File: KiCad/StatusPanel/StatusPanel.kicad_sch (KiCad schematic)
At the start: 1 part, among them U1 CC56-12EWA

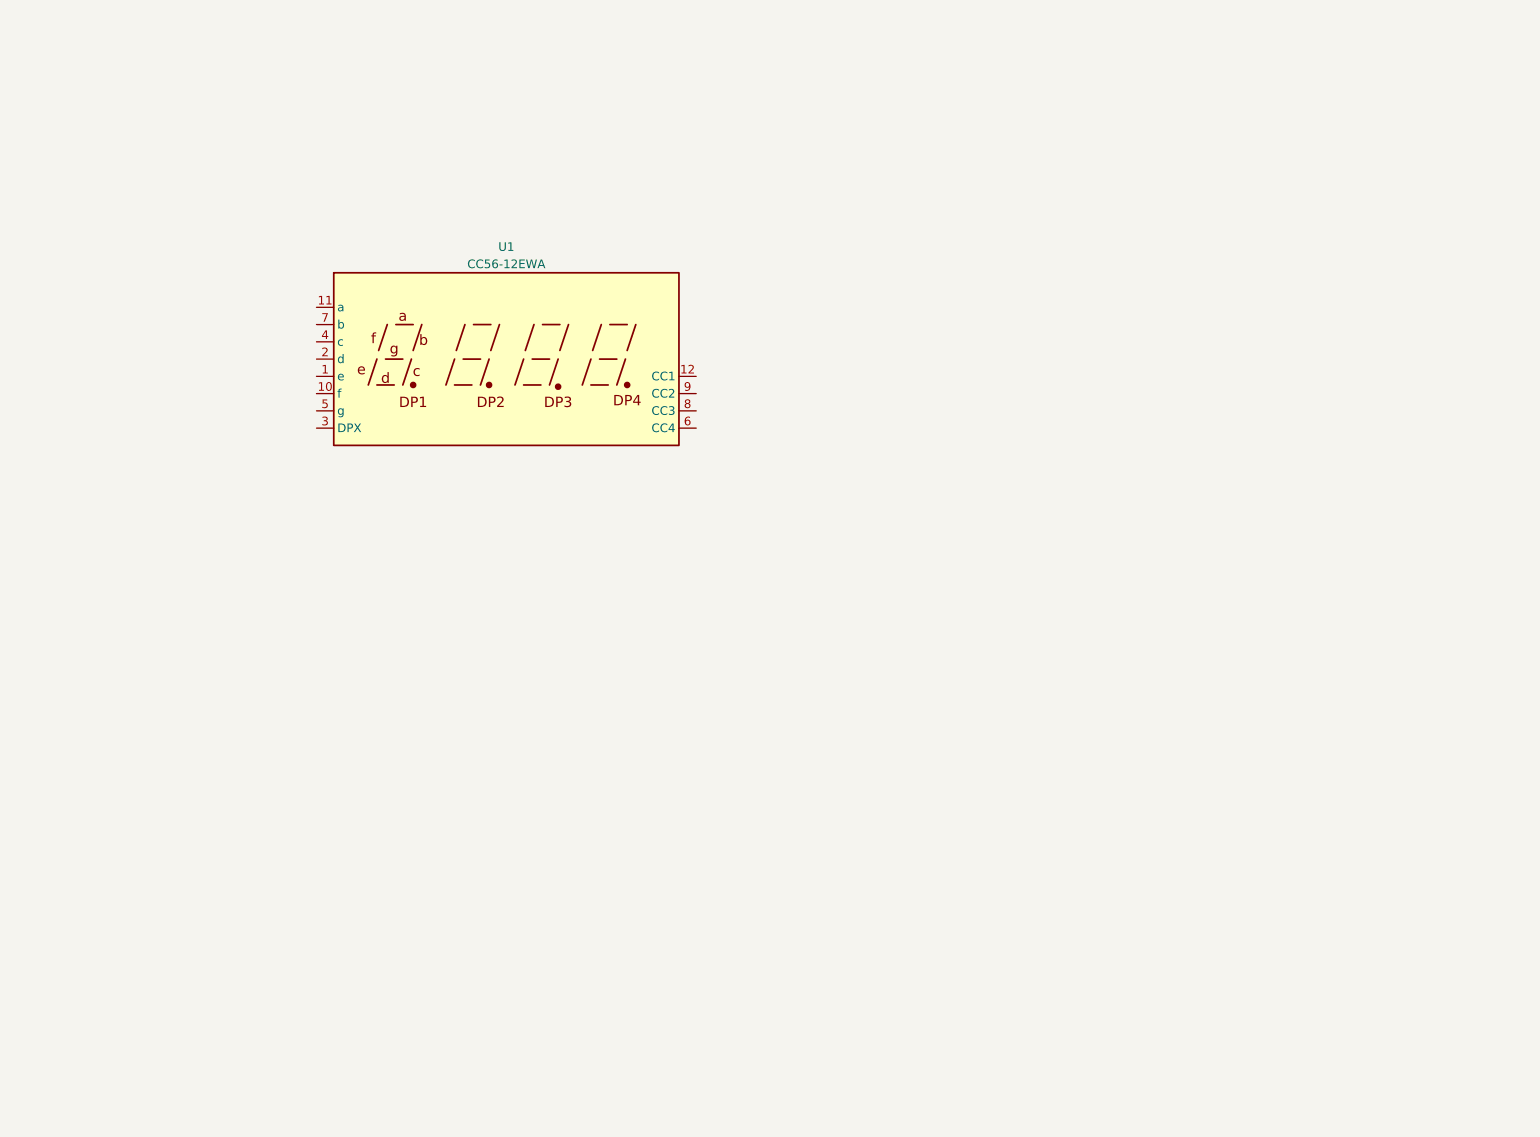
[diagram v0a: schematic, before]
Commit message: ステータスパネルの裏面に配線を追加
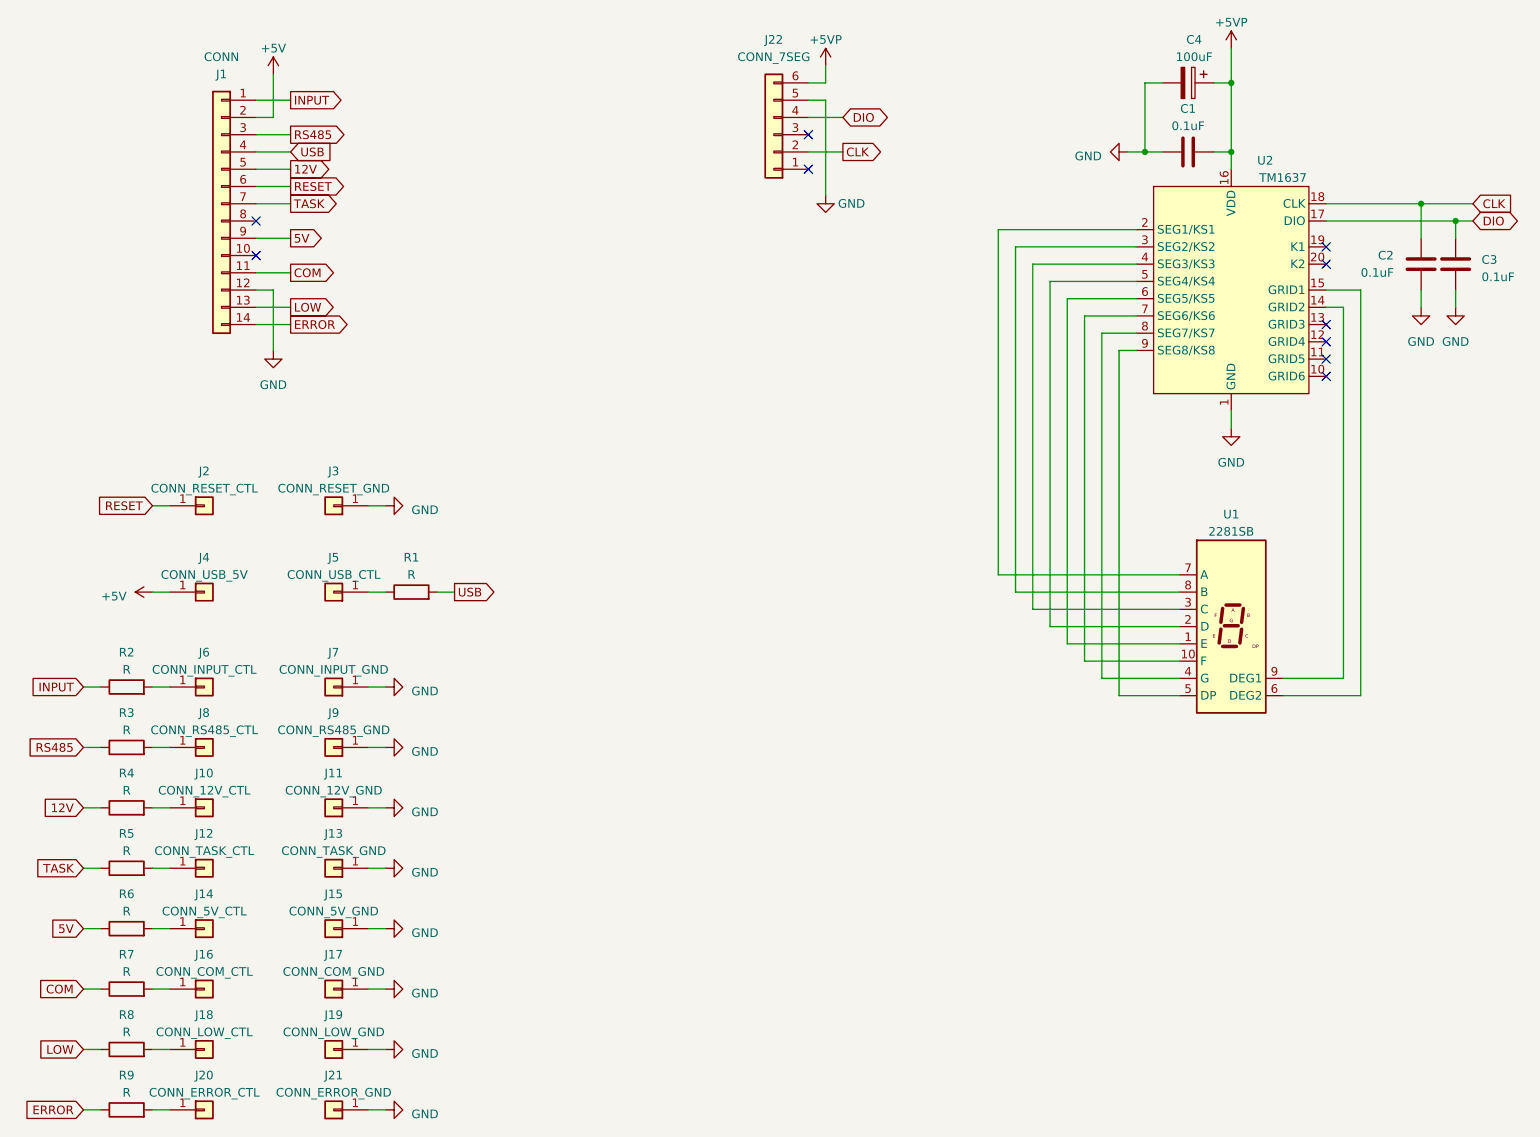
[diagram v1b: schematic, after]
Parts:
- removed U1: CC56-12EWA, Display_7Segment:CA56-12CGKWA, symbol Display_Character:CC56-12EWA
- added C1, C2, C3: 0.1uF, Capacitor_SMD:C_0603_1608Metric_Pad1.08x0.95mm_HandSolder, symbol Device:C
- added C4: 100uF, Capacitor_SMD:C_Elec_6.3x7.7, symbol Device:C_Polarized
- added J1: CONN, TSRP_Connector_Hirose:DF51A-14DP-2DS, symbol Connector_Generic:Conn_01x14
- added J10: CONN_12V_CTL, TSRP_Connector_Generic:1p, symbol Connector_Generic:Conn_01x01
- added J11: CONN_12V_GND, TSRP_Connector_Generic:1p, symbol Connector_Generic:Conn_01x01
- added J12: CONN_TASK_CTL, TSRP_Connector_Generic:1p, symbol Connector_Generic:Conn_01x01
- added J13: CONN_TASK_GND, TSRP_Connector_Generic:1p, symbol Connector_Generic:Conn_01x01
- added J14: CONN_5V_CTL, TSRP_Connector_Generic:1p, symbol Connector_Generic:Conn_01x01
- added J15: CONN_5V_GND, TSRP_Connector_Generic:1p, symbol Connector_Generic:Conn_01x01
- added J16: CONN_COM_CTL, TSRP_Connector_Generic:1p, symbol Connector_Generic:Conn_01x01
- added J17: CONN_COM_GND, TSRP_Connector_Generic:1p, symbol Connector_Generic:Conn_01x01
- added J18: CONN_LOW_CTL, TSRP_Connector_Generic:1p, symbol Connector_Generic:Conn_01x01
- added J19: CONN_LOW_GND, TSRP_Connector_Generic:1p, symbol Connector_Generic:Conn_01x01
- added J2: CONN_RESET_CTL, TSRP_Connector_Generic:1p, symbol Connector_Generic:Conn_01x01
- added J20: CONN_ERROR_CTL, TSRP_Connector_Generic:1p, symbol Connector_Generic:Conn_01x01
- added J21: CONN_ERROR_GND, TSRP_Connector_Generic:1p, symbol Connector_Generic:Conn_01x01
- added J22: CONN_7SEG, TSRP_Connector_Hirose:DF51A-6DP-2DSA, symbol Connector_Generic:Conn_01x06
- added J3: CONN_RESET_GND, TSRP_Connector_Generic:1p, symbol Connector_Generic:Conn_01x01
- added J4: CONN_USB_5V, TSRP_Connector_Generic:1p, symbol Connector_Generic:Conn_01x01
- added J5: CONN_USB_CTL, TSRP_Connector_Generic:1p, symbol Connector_Generic:Conn_01x01
- added J6: CONN_INPUT_CTL, TSRP_Connector_Generic:1p, symbol Connector_Generic:Conn_01x01
- added J7: CONN_INPUT_GND, TSRP_Connector_Generic:1p, symbol Connector_Generic:Conn_01x01
- added J8: CONN_RS485_CTL, TSRP_Connector_Generic:1p, symbol Connector_Generic:Conn_01x01
- added J9: CONN_RS485_GND, TSRP_Connector_Generic:1p, symbol Connector_Generic:Conn_01x01
- added R1, R2, R3, R4, R5, R6, R7, R8, R9: R, Resistor_SMD:R_0603_1608Metric_Pad0.98x0.95mm_HandSolder, symbol Device:R
- added U1: 2281SB, Display_7Segment:Sx39-1xxxxx, symbol Display_Character:SC39-12EWA
- added U2: TM1637, Package_SO:SOP-20_7.5x12.8mm_P1.27mm, symbol TSRP_Module:TM1637
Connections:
- new net: J6.1 (Pin_1), R2.2
- new net: J12.1 (Pin_1), R5.2
- new net: J20.1 (Pin_1), R9.2
- new net: J5.1 (Pin_1), R1.1
- new net: J14.1 (Pin_1), R6.2
- new net: J16.1 (Pin_1), R7.2
- new net: J8.1 (Pin_1), R3.2
- new net: J18.1 (Pin_1), R8.2
- new net: J10.1 (Pin_1), R4.2
- new net: U1.9 (DEG1), U2.14 (GRID2)
- new net: U1.6 (DEG2), U2.15 (GRID1)
- new net: U1.7 (A), U2.2 (SEG1/KS1)
- new net: U1.8 (B), U2.3 (SEG2/KS2)
- new net: U1.3 (C), U2.4 (SEG3/KS3)
- new net: U1.2 (D), U2.5 (SEG4/KS4)
- new net: U1.1 (E), U2.6 (SEG5/KS5)
- new net: U1.10 (F), U2.7 (SEG6/KS6)
- new net: U1.4 (G), U2.8 (SEG7/KS7)
- new net: U1.5 (DP), U2.9 (SEG8/KS8)
- new net +5V: J1.2 (Pin_2), J4.1 (Pin_1)
- new net +5VP: C1.2, C4.1, J22.6 (Pin_6), U2.16 (VDD)
- new net 12V: J1.5 (Pin_5), R4.1
- new net 5V: J1.9 (Pin_9), R6.1
- new net CLK: C2.2, J22.2 (Pin_2), U2.18 (CLK)
- new net COM: J1.11 (Pin_11), R7.1
- new net DIO: C3.2, J22.4 (Pin_4), U2.17 (DIO)
- new net ERROR: J1.14 (Pin_14), R9.1
- new net GND: C1.1, C2.1, C3.1, C4.2, J1.12 (Pin_12), J11.1 (Pin_1), J13.1 (Pin_1), J15.1 (Pin_1), J17.1 (Pin_1), J19.1 (Pin_1), J21.1 (Pin_1), J22.5 (Pin_5), J3.1 (Pin_1), J7.1 (Pin_1), J9.1 (Pin_1), U2.1 (GND)
- new net INPUT: J1.1 (Pin_1), R2.1
- new net LOW: J1.13 (Pin_13), R8.1
- new net RESET: J1.6 (Pin_6), J2.1 (Pin_1)
- new net RS485: J1.3 (Pin_3), R3.1
- new net TASK: J1.7 (Pin_7), R5.1
- new net USB: J1.4 (Pin_4), R1.2
- no-connect marks 0 -> 10

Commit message: 抵抗値を決定
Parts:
- R1, R2, R3, R4, R5, R6, R7, R8, R9: value R -> 270R
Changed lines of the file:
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@@
       (effects (font (size 1.27 1.27)))
     )
-    (property "Value" "R" (at 49.53 120.65 90)
+    (property "Value" "270R" (at 49.53 120.65 90)
       (effects (font (size 1.27 1.27)))
     )
@@
       (effects (font (size 1.27 1.27)))
     )
-    (property "Value" "R" (at 91.44 106.68 90)
+    (property "Value" "270R" (at 91.44 106.68 90)
       (effects (font (size 1.27 1.27)))
     )
@@
       (effects (font (size 1.27 1.27)))
     )
-    (property "Value" "R" (at 49.53 182.88 90)
+    (property "Value" "270R" (at 49.53 182.88 90)
       (effects (font (size 1.27 1.27)))
     )
@@
       (effects (font (size 1.27 1.27)))
     )
-    (property "Value" "R" (at 49.53 156.21 90)
+    (property "Value" "270R" (at 49.53 156.21 90)
       (effects (font (size 1.27 1.27)))
     )
@@
     (pin "14")
     (pin "15")
+    (pin "16")
     (pin "17")
-    (pin "16")
     (pin "18")
     (pin "19")
@@
       (effects (font (size 1.27 1.27)))
     )
-    (property "Value" "R" (at 49.53 165.1 90)
+    (property "Value" "270R" (at 49.53 165.1 90)
       (effects (font (size 1.27 1.27)))
     )
@@
       (effects (font (size 1.27 1.27)))
     )
-    (property "Value" "R" (at 49.53 129.54 90)
+    (property "Value" "270R" (at 49.53 129.54 90)
       (effects (font (size 1.27 1.27)))
     )
@@
       (effects (font (size 1.27 1.27)) hide)
     )
+    (pin "1")
+    (pin "10")
+    (pin "2")
+    (pin "3")
+    (pin "4")
+    (pin "5")
+    (pin "6")
+    (pin "7")
+    (pin "8")
     (pin "9")
-    (pin "7")
-    (pin "10")
-    (pin "4")
-    (pin "1")
-    (pin "2")
-    (pin "6")
-    (pin "5")
-    (pin "3")
-    (pin "8")
     (instances
       (project "StatusPanel"
@@
       (effects (font (size 1.27 1.27)))
     )
-    (property "Value" "R" (at 49.53 138.43 90)
+    (property "Value" "270R" (at 49.53 138.43 90)
       (effects (font (size 1.27 1.27)))
     )
@@
       (effects (font (size 1.27 1.27)))
     )
-    (property "Value" "R" (at 49.53 173.99 90)
+    (property "Value" "270R" (at 49.53 173.99 90)
       (effects (font (size 1.27 1.27)))
     )
@@
       (effects (font (size 1.27 1.27)))
     )
-    (property "Value" "R" (at 49.53 147.32 90)
-      (effects (font (size 1.27 1.27)))
-    )
+    (property "Value" "270R" (at 49.53 147.32 90)
+      (effects (font (size 1.27 1.27)))
+    )
